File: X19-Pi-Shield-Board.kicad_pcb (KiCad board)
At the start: 2 copper layers, 100 x 100 mm, 0 parts

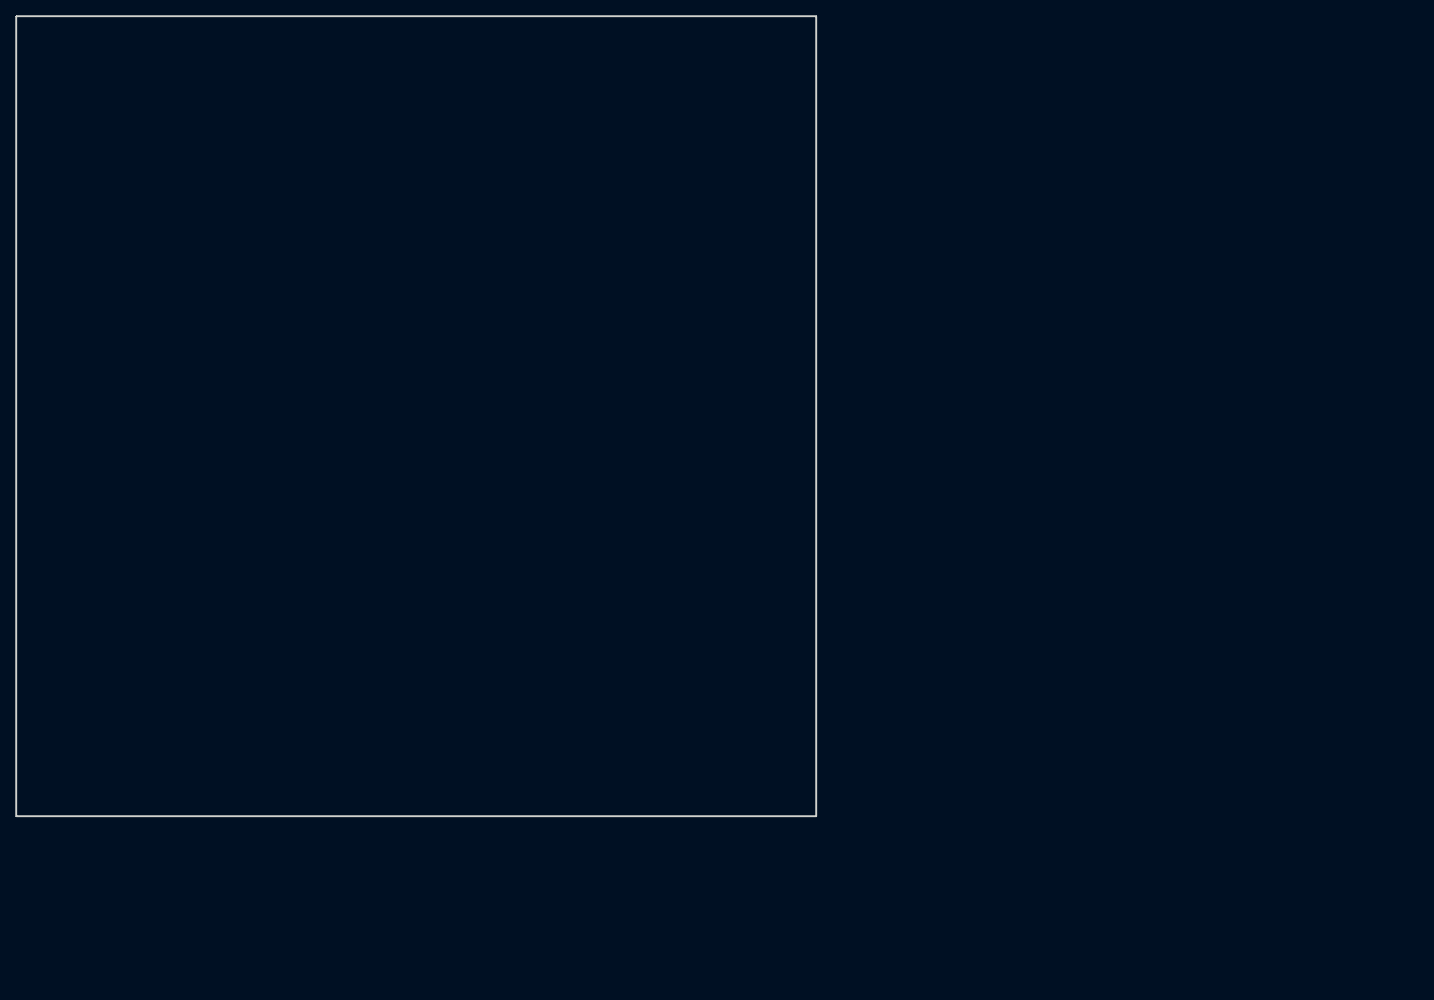
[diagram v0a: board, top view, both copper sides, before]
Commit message: adjust schematic and add board outline on pcb
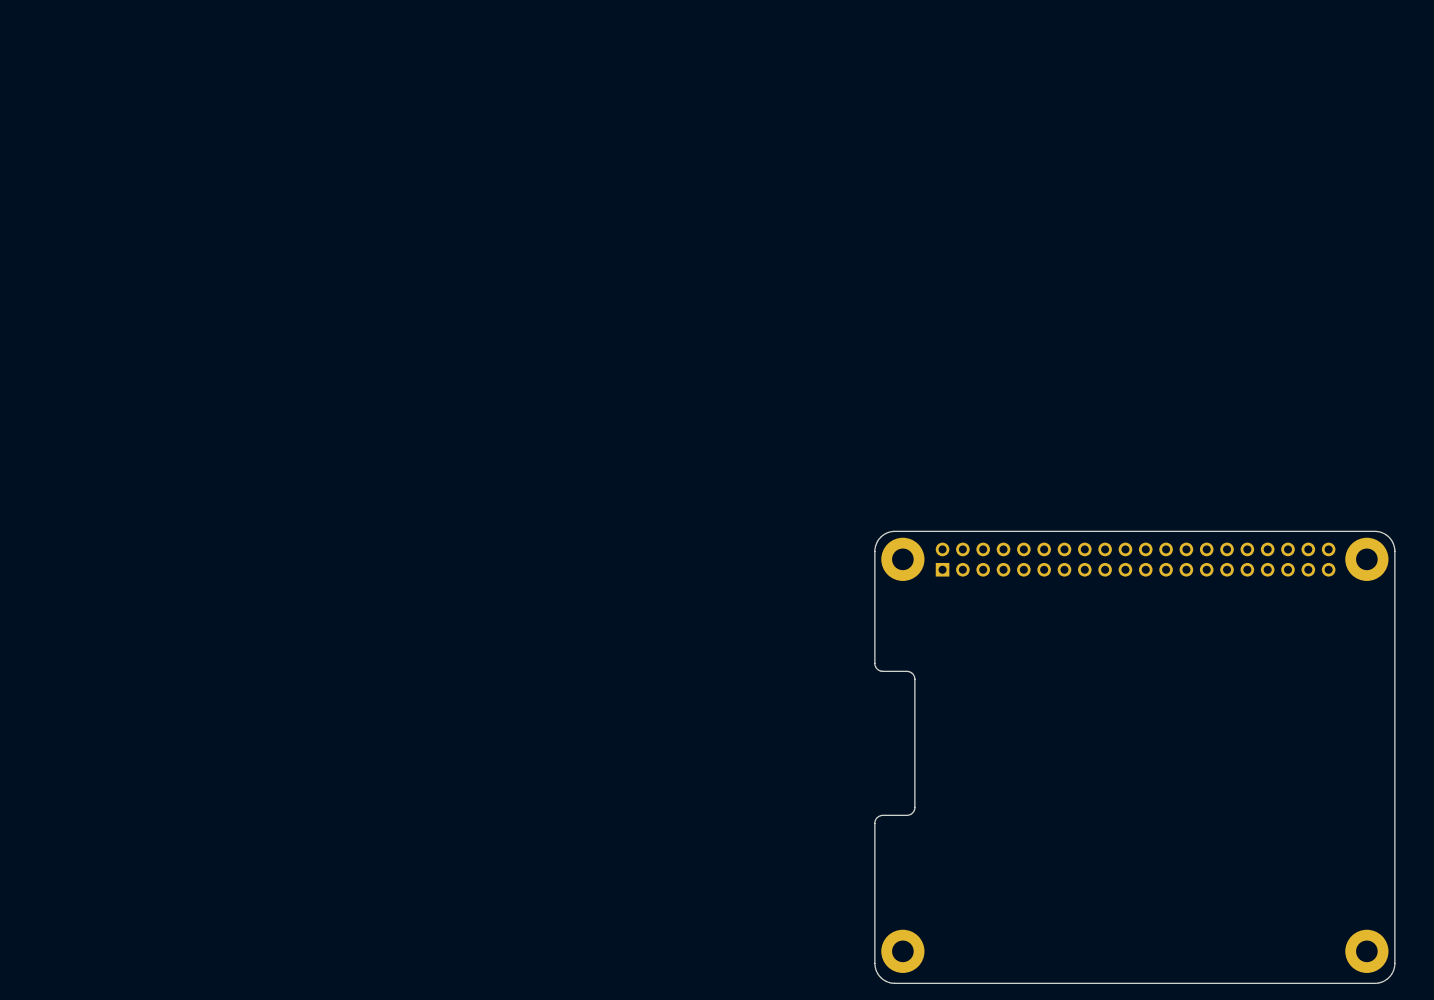
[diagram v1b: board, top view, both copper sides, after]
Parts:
- added H1: MountingHole_Pad, MountingHole:MountingHole_2.7mm_M2.5_Pad, F.Cu at (110.8, 67.9)
- added H2: MountingHole_Pad, MountingHole:MountingHole_2.7mm_M2.5_Pad, F.Cu at (168.8, 67.9)
- added H3: MountingHole_Pad, MountingHole:MountingHole_2.7mm_M2.5_Pad, F.Cu at (110.8, 116.9)
- added H4: MountingHole_Pad, MountingHole:MountingHole_2.7mm_M2.5_Pad, F.Cu at (168.8, 116.9)
- added J2: Raspberry_Pi_4, Connector_PinSocket_2.54mm:PinSocket_2x20_P2.54mm_Vertical, B.Cu at (115.8, 69.2)
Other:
- board size 100 x 100 mm -> 65 x 56.5 mm

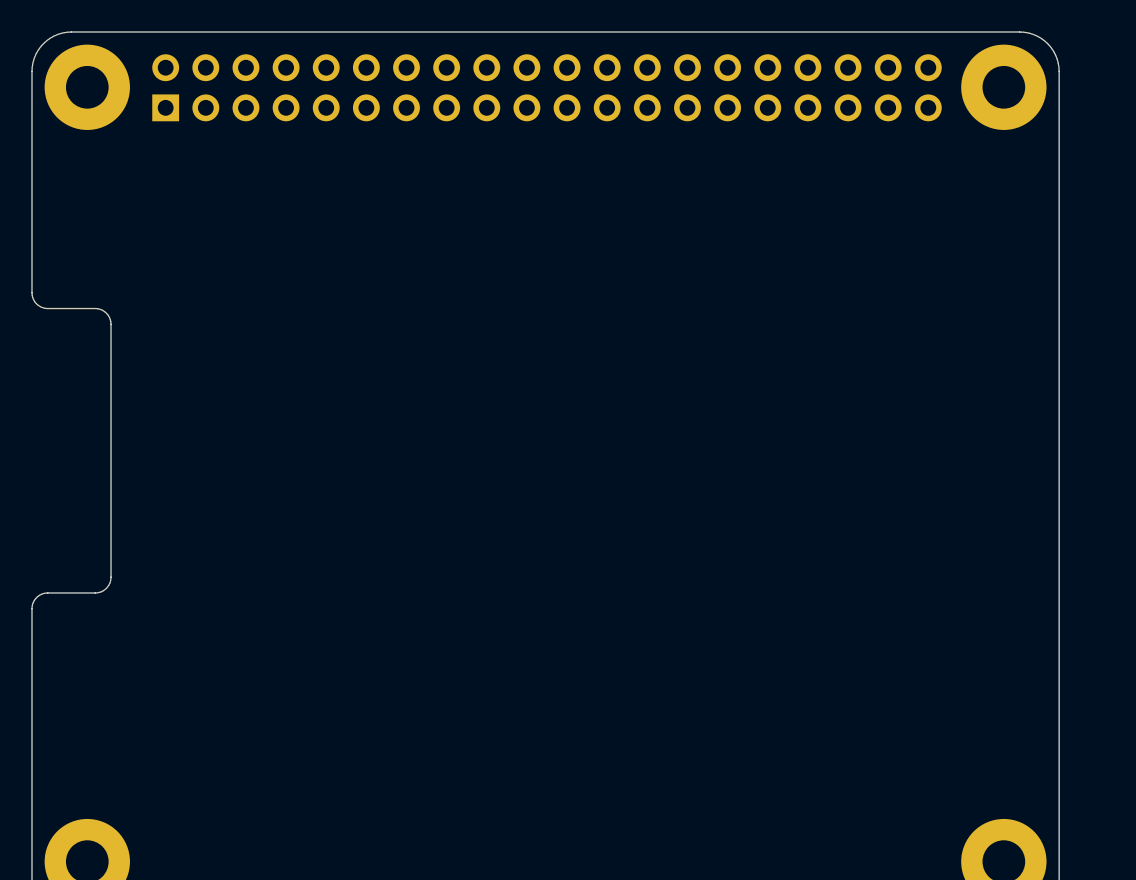
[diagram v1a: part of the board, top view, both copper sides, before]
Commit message: add connectors, mounting holes, fix some stuff
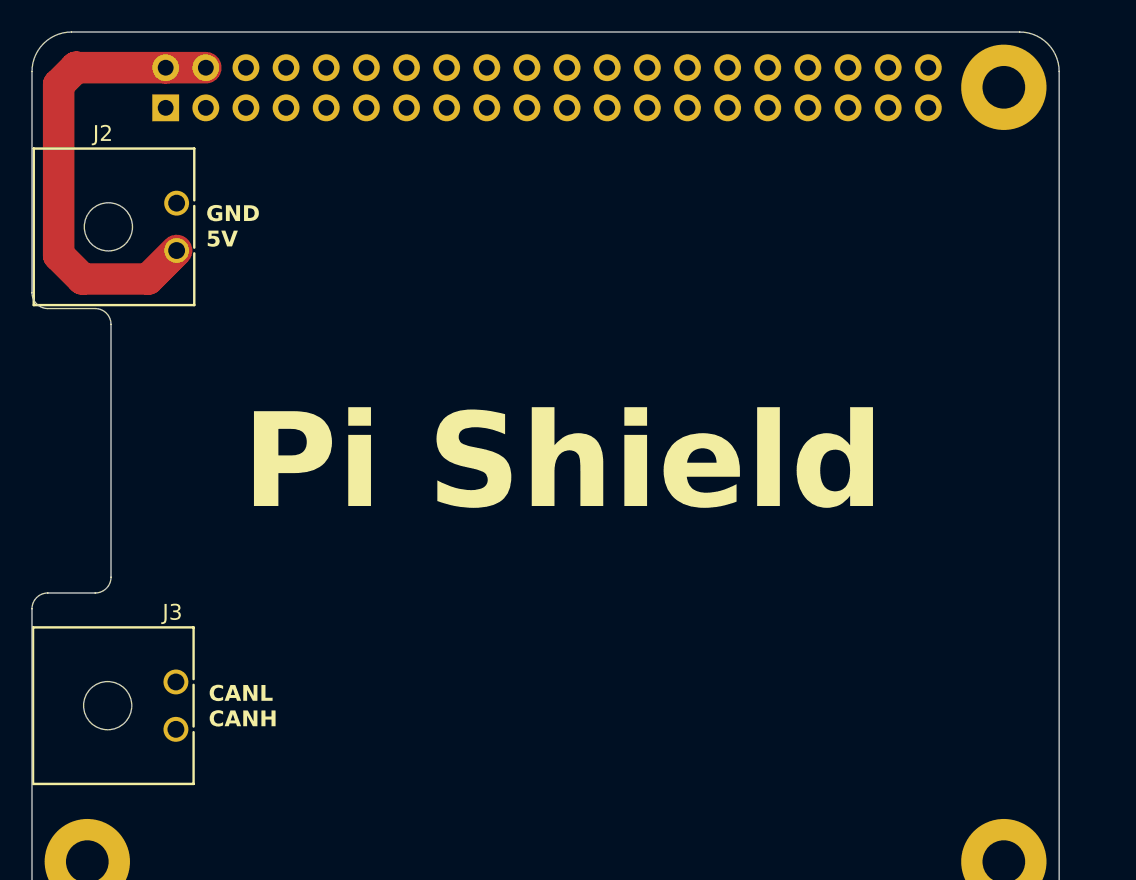
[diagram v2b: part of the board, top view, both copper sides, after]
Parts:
- removed the H1 at (110.8, 67.9)
- added J1: Raspberry_Pi_4, Connector_PinSocket_2.54mm:PinSocket_2x20_P2.54mm_Vertical, B.Cu at (115.8, 69.2)
- added J3: Conn_01x02, rov_connectors:0436500200, F.Cu at (116.4, 108.5)
- J2: value Raspberry_Pi_4 -> Conn_01x02; footprint Connector_PinSocket_2.54mm:PinSocket_2x20_P2.54mm_Vertical -> rov_connectors:0436500200; moved to F.Cu
- moved J2 9.06 mm to (116.5, 78.2)
- renumbered H2 to H1, H4 to H2
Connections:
- J2 pad 1: Net-(J2-3V3-Pad1) -> /5V_PI
- J2 pad 2: Net-(J2-5V-Pad2) -> GND
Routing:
- net /5V_PI: track 0.00 -> 29.4 mm
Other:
- board text added: "CANL CANH"
- board text added: "GND 5V"
- board text added: "Pi Shield"
